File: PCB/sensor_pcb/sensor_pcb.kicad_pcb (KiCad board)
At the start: 2 copper layers, 17.8 x 24.1 mm, 3 parts, among them P1 CONN_01X03, Q1 BUT11A, Q2 BUT11A

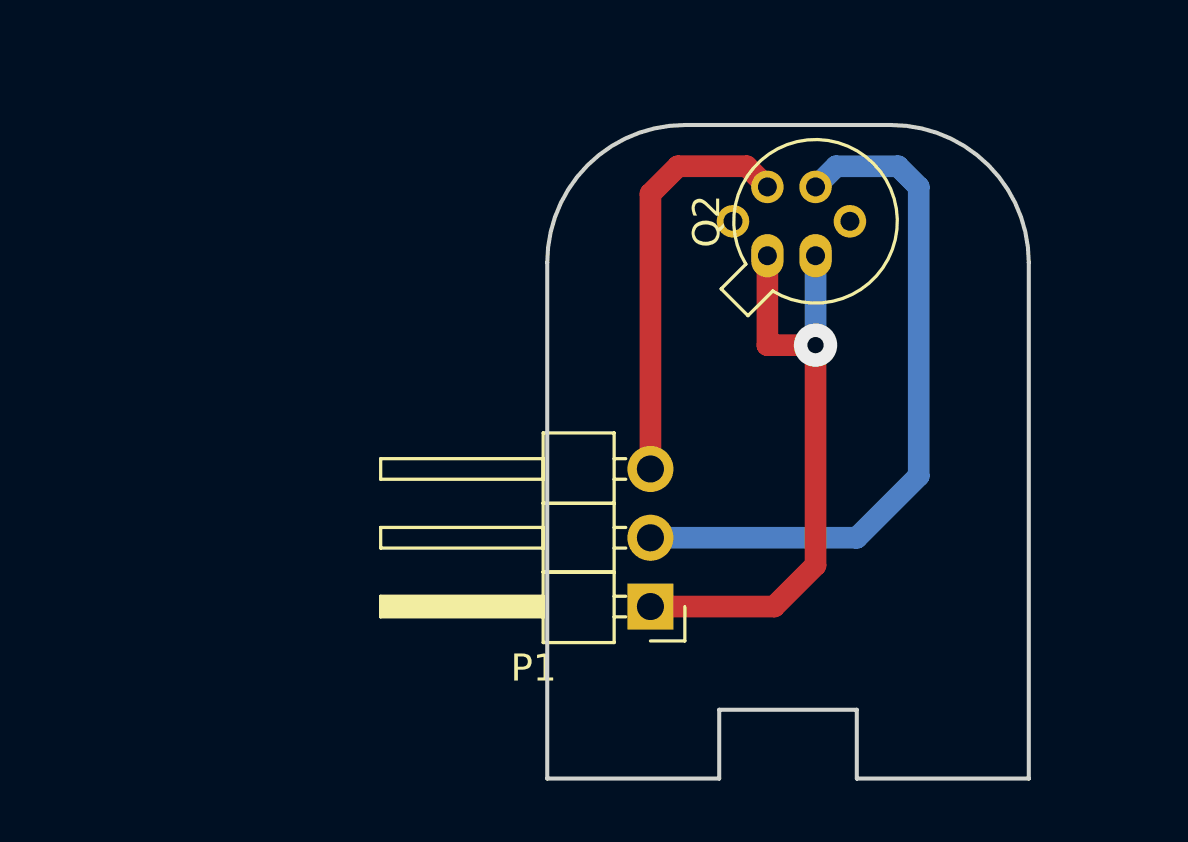
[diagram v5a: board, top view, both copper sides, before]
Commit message: Sensor pcb redesign.  Fixed bug where teensy would freeze if there were more than 10 targets
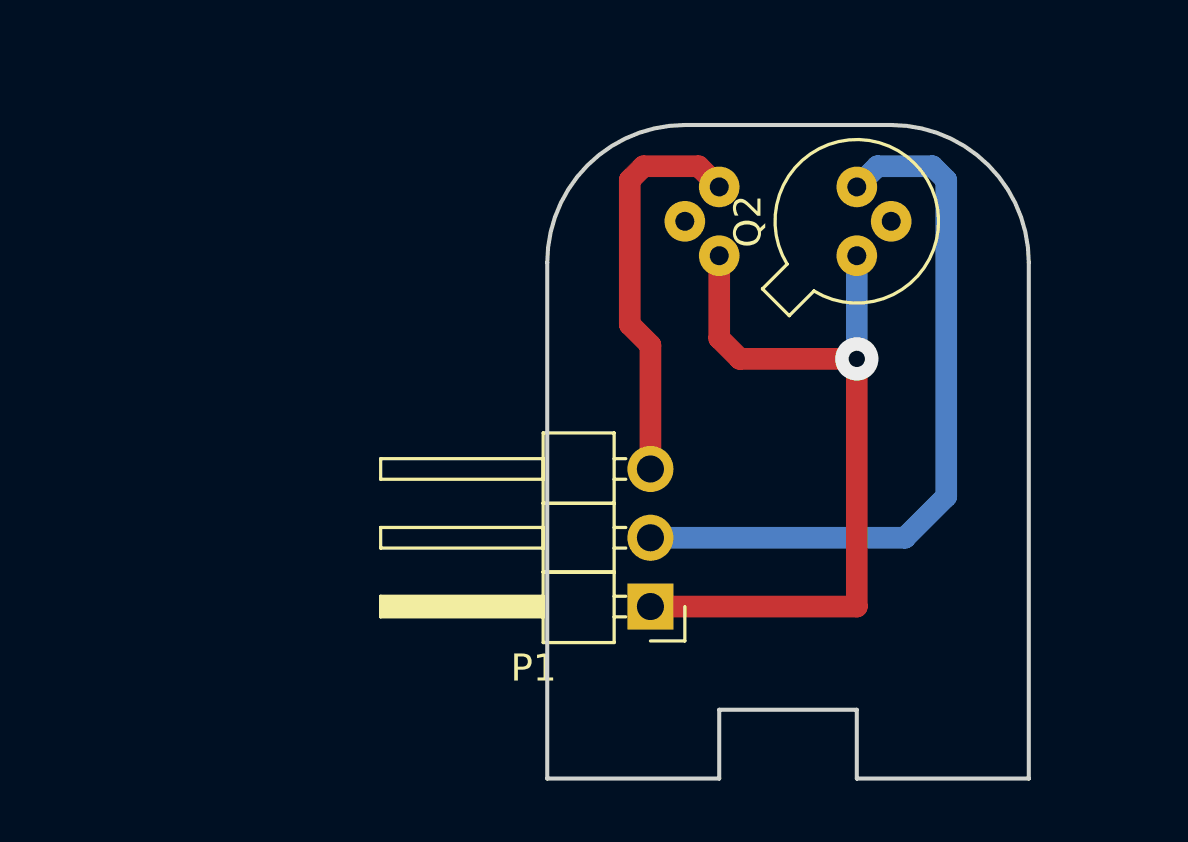
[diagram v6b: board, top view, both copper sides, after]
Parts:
- moved Q1 1.78 mm to (157.5, 106.4)
- moved Q2 1.52 mm to (162.6, 106.4)
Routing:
- net Net-(P1-Pad1): track 23.2 -> 29.0 mm
- net Net-(P1-Pad2): track 26.0 -> 27.1 mm
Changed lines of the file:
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@@
     (thickness 1.6)
     (drawings 13)
-    (tracks 17)
+    (tracks 19)
     (zones 0)
     (modules 3)
@@
     (mod_text_size 1 1)
     (mod_text_width 0.15)
-    (pad_size 1.6 1.2)
+    (pad_size 1.5 1.5)
     (pad_drill 0.7)
     (pad_to_mask_clearance 0.2)
@@
   )
   (module TO_SOT_Packages_THT:TO-18-3_Lens (layer B.Cu)
-    (at 159.258 106.426 90)
+    (at 157.48 106.426 90)
     (descr "TO-18-3_Lens, Lens")
     (tags "TO-18-3_Lens Lens")
@@
     (fp_arc (start 1.27 0) (end -0.329057 2.419301) (angle -336.9) (layer B.Fab) (width 0.1))
     (fp_arc (start 1.27 0) (end -0.312331 2.572281) (angle -333.2) (layer B.SilkS) (width 0.12))
-    (pad 3 thru_hole oval (at 0 0 90) (size 1.6 1.2) (drill 0.7) (layers *.Cu *.Mask)
+    (pad 3 thru_hole oval (at 0 0 90) (size 1.5 1.5) (drill 0.7) (layers *.Cu *.Mask)
       (net 1 "Net-(P1-Pad1)"))
-    (pad 1 thru_hole oval (at 1.27 -1.27 90) (size 1.2 1.2) (drill 0.7) (layers *.Cu *.Mask)
+    (pad 1 thru_hole oval (at 1.27 -1.27 90) (size 1.5 1.5) (drill 0.7) (layers *.Cu *.Mask)
       (net 4 "Net-(Q1-Pad1)"))
-    (pad 2 thru_hole oval (at 2.54 0 90) (size 1.2 1.2) (drill 0.7) (layers *.Cu *.Mask)
+    (pad 2 thru_hole oval (at 2.54 0 90) (size 1.5 1.5) (drill 0.7) (layers *.Cu *.Mask)
       (net 3 "Net-(P1-Pad3)"))
     (model ${KISYS3DMOD}/TO_SOT_Packages_THT.3dshapes/TO-18-3_Lens.wrl
@@
   )
   (module TO_SOT_Packages_THT:TO-18-3_Lens (layer F.Cu)
-    (at 161.036 106.426 90)
+    (at 162.56 106.426 90)
     (descr "TO-18-3_Lens, Lens")
     (tags "TO-18-3_Lens Lens")
@@
     (fp_arc (start 1.27 0) (end -0.329057 -2.419301) (angle 336.9) (layer F.Fab) (width 0.1))
     (fp_arc (start 1.27 0) (end -0.312331 -2.572281) (angle 333.2) (layer F.SilkS) (width 0.12))
-    (pad 3 thru_hole oval (at 0 0 90) (size 1.6 1.2) (drill 0.7) (layers *.Cu *.Mask)
+    (pad 3 thru_hole oval (at 0 0 90) (size 1.5 1.5) (drill 0.7) (layers *.Cu *.Mask)
       (net 1 "Net-(P1-Pad1)"))
-    (pad 1 thru_hole oval (at 1.27 1.27 90) (size 1.2 1.2) (drill 0.7) (layers *.Cu *.Mask)
+    (pad 1 thru_hole oval (at 1.27 1.27 90) (size 1.5 1.5) (drill 0.7) (layers *.Cu *.Mask)
       (net 5 "Net-(Q2-Pad1)"))
-    (pad 2 thru_hole oval (at 2.54 0 90) (size 1.2 1.2) (drill 0.7) (layers *.Cu *.Mask)
+    (pad 2 thru_hole oval (at 2.54 0 90) (size 1.5 1.5) (drill 0.7) (layers *.Cu *.Mask)
       (net 2 "Net-(P1-Pad2)"))
     (model ${KISYS3DMOD}/TO_SOT_Packages_THT.3dshapes/TO-18-3_Lens.wrl
@@
   (gr_line (start 157.48 123.19) (end 162.56 123.19) (angle 90) (layer Edge.Cuts) (width 0.15))
   (gr_line (start 157.48 125.73) (end 157.48 123.19) (angle 90) (layer Edge.Cuts) (width 0.15))
-  (segment (start 161.036 109.728) (end 159.258 109.728) (width 0.8) (layer F.Cu) (net 1))
-  (segment (start 159.258 109.728) (end 159.258 106.426) (width 0.8) (layer F.Cu) (net 1))
-  (segment (start 154.94 119.38) (end 159.512 119.38) (width 0.8) (layer F.Cu) (net 1))
-  (segment (start 161.036 109.728) (end 161.036 106.426) (width 0.8) (layer B.Cu) (net 1))
-  (via (at 161.036 109.728) (size 1.6) (drill 0.6) (layers F.Cu B.Cu) (net 1))
-  (segment (start 161.036 117.856) (end 161.036 109.728) (width 0.8) (layer F.Cu) (net 1))
-  (segment (start 159.512 119.38) (end 161.036 117.856) (width 0.8) (layer F.Cu) (net 1))
-  (segment (start 154.94 116.84) (end 162.56 116.84) (width 0.8) (layer B.Cu) (net 2))
-  (segment (start 161.798 103.124) (end 161.036 103.886) (width 0.8) (layer B.Cu) (net 2))
-  (segment (start 164.084 103.124) (end 161.798 103.124) (width 0.8) (layer B.Cu) (net 2))
-  (segment (start 164.846 103.886) (end 164.084 103.124) (width 0.8) (layer B.Cu) (net 2))
-  (segment (start 164.846 114.554) (end 164.846 103.886) (width 0.8) (layer B.Cu) (net 2))
-  (segment (start 162.56 116.84) (end 164.846 114.554) (width 0.8) (layer B.Cu) (net 2))
-  (segment (start 154.94 114.3) (end 154.94 104.14) (width 0.8) (layer F.Cu) (net 3))
-  (segment (start 158.496 103.124) (end 159.258 103.886) (width 0.8) (layer F.Cu) (net 3))
-  (segment (start 155.956 103.124) (end 158.496 103.124) (width 0.8) (layer F.Cu) (net 3))
-  (segment (start 154.94 104.14) (end 155.956 103.124) (width 0.8) (layer F.Cu) (net 3))
+  (segment (start 162.56 110.236) (end 158.242 110.236) (width 0.8) (layer F.Cu) (net 1))
+  (segment (start 157.48 109.474) (end 157.48 106.426) (width 0.8) (layer F.Cu) (net 1) (status 800000))
+  (segment (start 158.242 110.236) (end 157.48 109.474) (width 0.8) (layer F.Cu) (net 1))
+  (segment (start 154.94 119.38) (end 162.56 119.38) (width 0.8) (layer F.Cu) (net 1) (status 400000))
+  (segment (start 162.56 110.236) (end 162.56 106.426) (width 0.8) (layer B.Cu) (net 1) (status 800000))
+  (via (at 162.56 110.236) (size 1.6) (drill 0.6) (layers F.Cu B.Cu) (net 1))
+  (segment (start 162.56 119.38) (end 162.56 110.236) (width 0.8) (layer F.Cu) (net 1))
+  (segment (start 154.94 116.84) (end 164.338 116.84) (width 0.8) (layer B.Cu) (net 2) (status 400000))
+  (segment (start 163.322 103.124) (end 162.56 103.886) (width 0.8) (layer B.Cu) (net 2) (status 800000))
+  (segment (start 165.354 103.124) (end 163.322 103.124) (width 0.8) (layer B.Cu) (net 2))
+  (segment (start 165.862 103.632) (end 165.354 103.124) (width 0.8) (layer B.Cu) (net 2))
+  (segment (start 165.862 115.316) (end 165.862 103.632) (width 0.8) (layer B.Cu) (net 2))
+  (segment (start 164.338 116.84) (end 165.862 115.316) (width 0.8) (layer B.Cu) (net 2))
+  (segment (start 154.94 114.3) (end 154.94 109.728) (width 0.8) (layer F.Cu) (net 3) (status 400000))
+  (segment (start 156.718 103.124) (end 157.48 103.886) (width 0.8) (layer F.Cu) (net 3) (status 800000))
+  (segment (start 154.686 103.124) (end 156.718 103.124) (width 0.8) (layer F.Cu) (net 3))
+  (segment (start 154.178 103.632) (end 154.686 103.124) (width 0.8) (layer F.Cu) (net 3))
+  (segment (start 154.178 108.966) (end 154.178 103.632) (width 0.8) (layer F.Cu) (net 3))
+  (segment (start 154.94 109.728) (end 154.178 108.966) (width 0.8) (layer F.Cu) (net 3))
 )

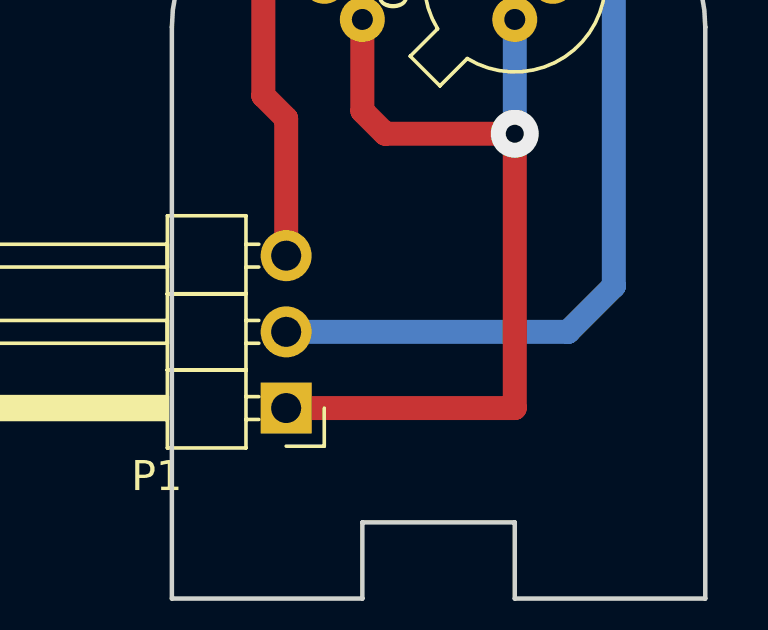
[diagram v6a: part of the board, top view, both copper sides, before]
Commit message: Updated simulator to work with fixed coordinate system in hardware
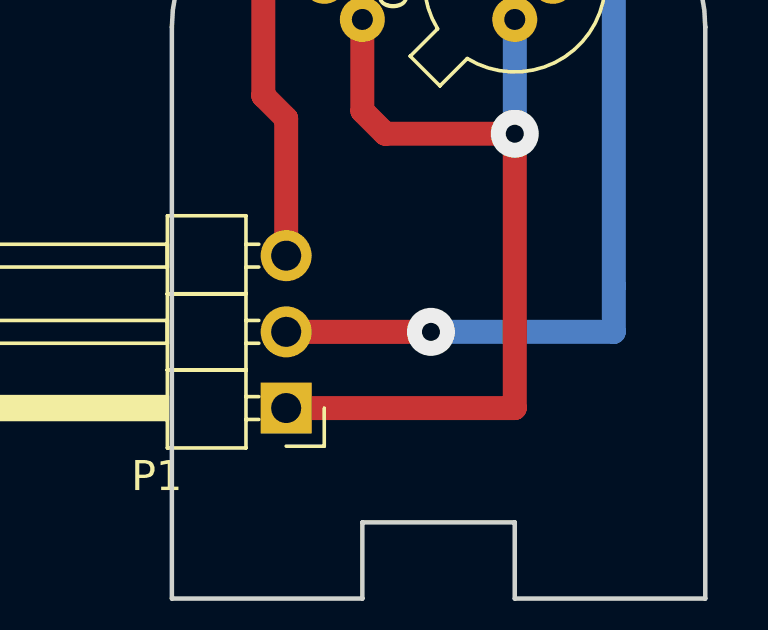
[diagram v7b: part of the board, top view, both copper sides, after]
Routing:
- net Net-(P1-Pad2): track 27.1 -> 28.0 mm, vias 0 -> 1
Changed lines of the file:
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@@
-(kicad_pcb (version 4) (host pcbnew 4.0.2-stable)
+(kicad_pcb (version 4) (host pcbnew 4.0.6)
   (general
     (links 4)
     (no_connects 0)
-    (area 144.314999 94.94 184.53 132.240001)
+    (area 144.314999 95.09 184.38 132.240001)
     (thickness 1.6)
     (drawings 13)
-    (tracks 19)
+    (tracks 21)
     (zones 0)
     (modules 3)
@@
   (gr_line (start 157.48 125.73) (end 157.48 123.19) (angle 90) (layer Edge.Cuts) (width 0.15))
   (segment (start 162.56 110.236) (end 158.242 110.236) (width 0.8) (layer F.Cu) (net 1))
-  (segment (start 157.48 109.474) (end 157.48 106.426) (width 0.8) (layer F.Cu) (net 1) (status 800000))
+  (segment (start 157.48 109.474) (end 157.48 106.426) (width 0.8) (layer F.Cu) (net 1))
   (segment (start 158.242 110.236) (end 157.48 109.474) (width 0.8) (layer F.Cu) (net 1))
-  (segment (start 154.94 119.38) (end 162.56 119.38) (width 0.8) (layer F.Cu) (net 1) (status 400000))
-  (segment (start 162.56 110.236) (end 162.56 106.426) (width 0.8) (layer B.Cu) (net 1) (status 800000))
+  (segment (start 154.94 119.38) (end 162.56 119.38) (width 0.8) (layer F.Cu) (net 1))
+  (segment (start 162.56 110.236) (end 162.56 106.426) (width 0.8) (layer B.Cu) (net 1))
   (via (at 162.56 110.236) (size 1.6) (drill 0.6) (layers F.Cu B.Cu) (net 1))
   (segment (start 162.56 119.38) (end 162.56 110.236) (width 0.8) (layer F.Cu) (net 1))
-  (segment (start 154.94 116.84) (end 164.338 116.84) (width 0.8) (layer B.Cu) (net 2) (status 400000))
-  (segment (start 163.322 103.124) (end 162.56 103.886) (width 0.8) (layer B.Cu) (net 2) (status 800000))
+  (segment (start 154.94 116.84) (end 159.766 116.84) (width 0.8) (layer F.Cu) (net 2) (status 400000))
+  (segment (start 165.862 115.316) (end 165.862 103.632) (width 0.8) (layer B.Cu) (net 2))
+  (segment (start 165.862 103.632) (end 165.354 103.124) (width 0.8) (layer B.Cu) (net 2))
   (segment (start 165.354 103.124) (end 163.322 103.124) (width 0.8) (layer B.Cu) (net 2))
-  (segment (start 165.862 103.632) (end 165.354 103.124) (width 0.8) (layer B.Cu) (net 2))
-  (segment (start 165.862 115.316) (end 165.862 103.632) (width 0.8) (layer B.Cu) (net 2))
-  (segment (start 164.338 116.84) (end 165.862 115.316) (width 0.8) (layer B.Cu) (net 2))
-  (segment (start 154.94 114.3) (end 154.94 109.728) (width 0.8) (layer F.Cu) (net 3) (status 400000))
-  (segment (start 156.718 103.124) (end 157.48 103.886) (width 0.8) (layer F.Cu) (net 3) (status 800000))
+  (segment (start 163.322 103.124) (end 162.56 103.886) (width 0.8) (layer B.Cu) (net 2))
+  (segment (start 165.862 116.84) (end 165.862 115.316) (width 0.8) (layer B.Cu) (net 2))
+  (segment (start 159.766 116.84) (end 165.862 116.84) (width 0.8) (layer B.Cu) (net 2))
+  (via (at 159.766 116.84) (size 1.6) (drill 0.6) (layers F.Cu B.Cu) (net 2))
+  (segment (start 154.94 114.3) (end 154.94 109.728) (width 0.8) (layer F.Cu) (net 3))
+  (segment (start 156.718 103.124) (end 157.48 103.886) (width 0.8) (layer F.Cu) (net 3))
   (segment (start 154.686 103.124) (end 156.718 103.124) (width 0.8) (layer F.Cu) (net 3))
   (segment (start 154.178 103.632) (end 154.686 103.124) (width 0.8) (layer F.Cu) (net 3))
